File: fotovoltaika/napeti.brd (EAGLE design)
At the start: 46.7 x 49.5 mm, 15 parts, among them X5 JST-XH-04-PIN-LONG-PAD

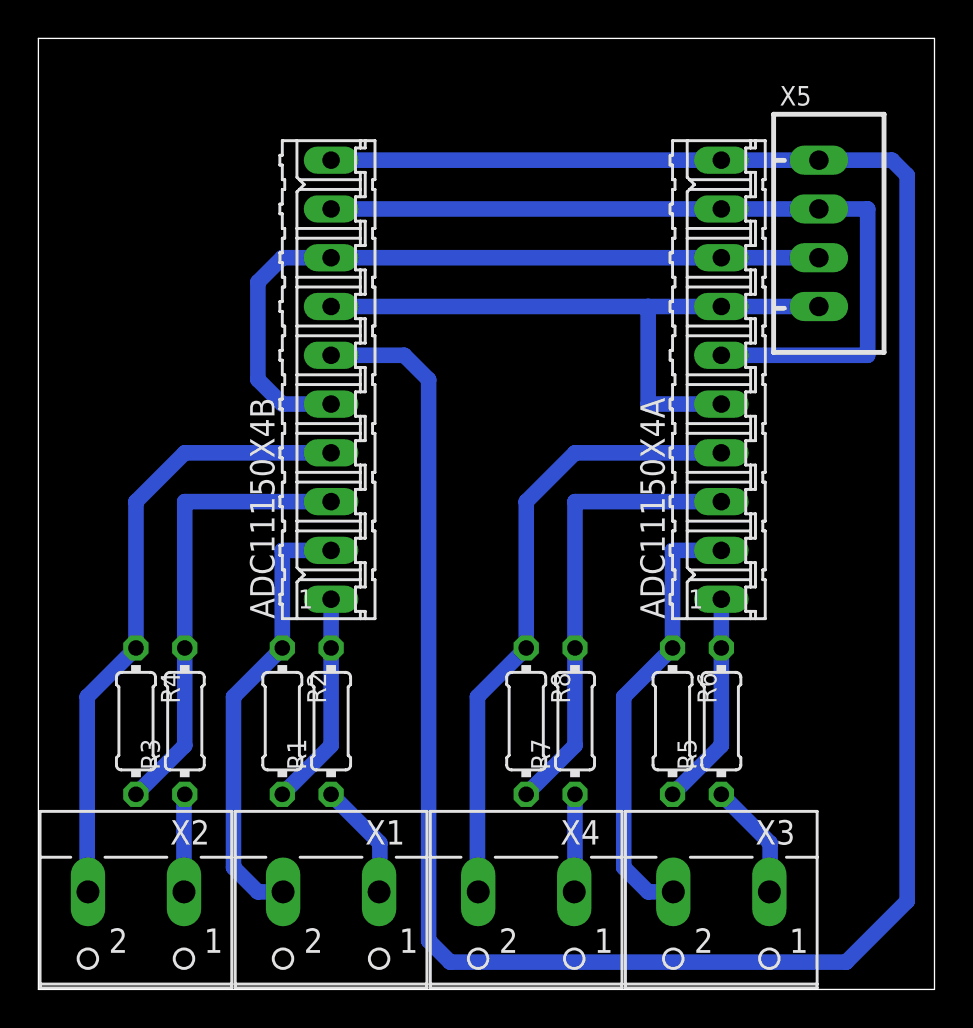
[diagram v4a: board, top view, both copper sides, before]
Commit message: zmena na konektory JST-XH
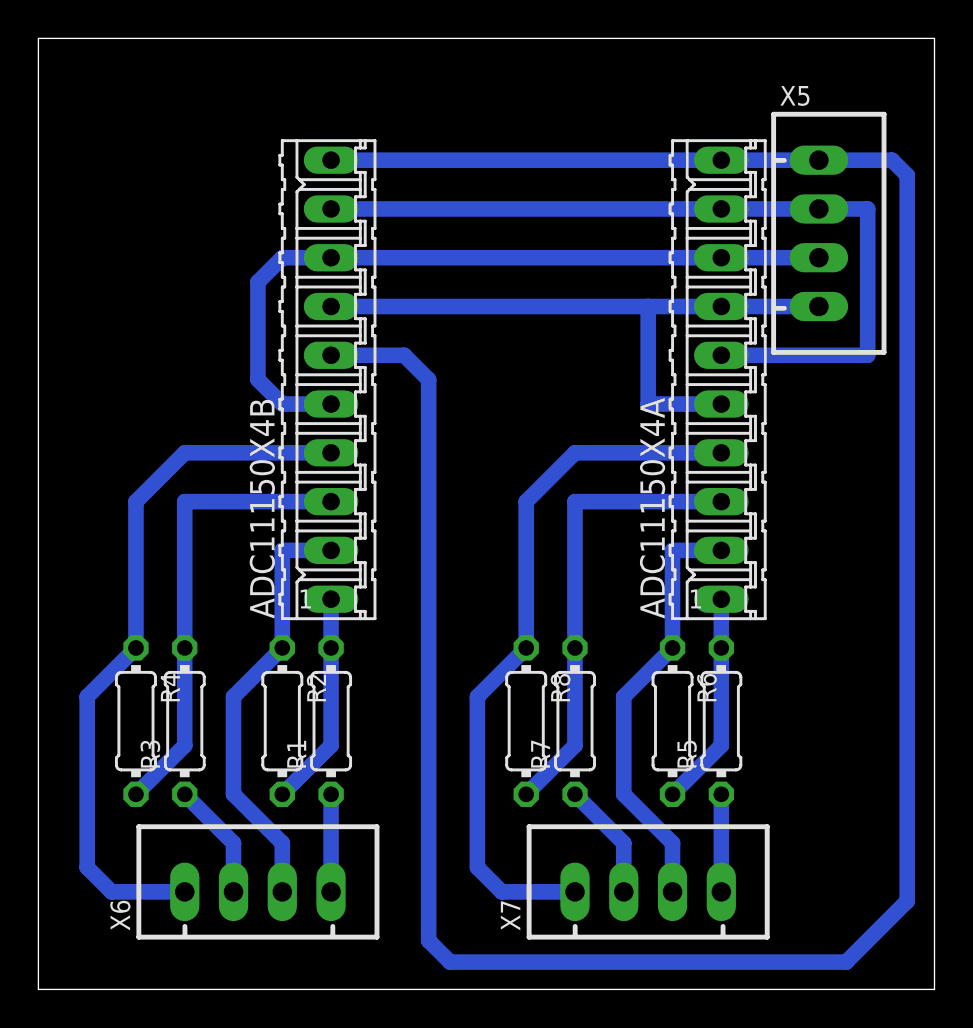
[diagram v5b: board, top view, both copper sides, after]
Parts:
- removed X1, X2, X3, X4: (no value), con-wago-500:W237-102
- added X6, X7: JST-XH-04-PIN-LONG-PAD, Rembrandt:JST-XH-04-PACKAGE-LONG-PAD
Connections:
- net N$10: now also X6.3; no longer X1.2
- net N$14: now also X6.1; no longer X2.2
- net N$2: now also X6.4; no longer X1.1
- net N$3: now also X7.3; no longer X3.2
- net N$5: now also X6.2; no longer X2.1
- net N$6: now also X7.1; no longer X4.2
- net N$7: now also X7.4; no longer X3.1
- net N$8: now also X7.2; no longer X4.1
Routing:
- net N$6: track 32.6 -> 36.9 mm
- net N$14: track 32.6 -> 36.9 mm
- net N$2: track 6.17 -> 5.08 mm
- net N$7: track 6.15 -> 5.08 mm
- net N$5: track 5.10 -> 6.13 mm
- net N$8: track 5.10 -> 6.13 mm
- net N$3: track 23.2 -> 22.4 mm
- net N$10: track 23.2 -> 22.4 mm
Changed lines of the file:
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@@
 <attribute name="VALUE" x="24.9174" y="15.5956" size="0.9906" layer="27" ratio="10" rot="R270"/>
-</element>
-<element name="X1" library="con-wago-500" library_urn="urn:adsk.eagle:library:195" package="W237-102" package3d_urn="urn:adsk.eagle:package:10688/1" value="" x="15.24" y="3.81" smashed="yes" rot="R180">
-<attribute name="MF" value="" x="15.24" y="3.81" size="1.778" layer="27" rot="R180" display="off"/>
-<attribute name="MPN" value="237-102" x="15.24" y="3.81" size="1.778" layer="27" rot="R180" display="off"/>
-<attribute name="NAME" x="19.0862" y="8.8138" size="1.27" layer="25" ratio="10" rot="R180"/>
-<attribute name="OC_FARNELL" value="unknown" x="15.24" y="3.81" size="1.778" layer="27" rot="R180" display="off"/>
-<attribute name="OC_NEWARK" value="70K9898" x="15.24" y="3.81" size="1.778" layer="27" rot="R180" display="off"/>
-<attribute name="VALUE" x="20.28" y="11.43" size="1.27" layer="27" ratio="10" rot="R180"/>
-</element>
-<element name="X2" library="con-wago-500" library_urn="urn:adsk.eagle:library:195" package="W237-102" package3d_urn="urn:adsk.eagle:package:10688/1" value="" x="5.08" y="3.81" smashed="yes" rot="R180">
-<attribute name="MF" value="" x="5.08" y="3.81" size="1.778" layer="27" rot="R180" display="off"/>
-<attribute name="MPN" value="237-102" x="5.08" y="3.81" size="1.778" layer="27" rot="R180" display="off"/>
-<attribute name="NAME" x="8.9262" y="8.8138" size="1.27" layer="25" ratio="10" rot="R180"/>
-<attribute name="OC_FARNELL" value="unknown" x="5.08" y="3.81" size="1.778" layer="27" rot="R180" display="off"/>
-<attribute name="OC_NEWARK" value="70K9898" x="5.08" y="3.81" size="1.778" layer="27" rot="R180" display="off"/>
-<attribute name="VALUE" x="10.12" y="11.43" size="1.27" layer="27" ratio="10" rot="R180"/>
-</element>
-<element name="X3" library="con-wago-500" library_urn="urn:adsk.eagle:library:195" package="W237-102" package3d_urn="urn:adsk.eagle:package:10688/1" value="" x="35.56" y="3.81" smashed="yes" rot="R180">
-<attribute name="MF" value="" x="35.56" y="3.81" size="1.778" layer="27" rot="R180" display="off"/>
-<attribute name="MPN" value="237-102" x="35.56" y="3.81" size="1.778" layer="27" rot="R180" display="off"/>
-<attribute name="NAME" x="39.4062" y="8.8138" size="1.27" layer="25" ratio="10" rot="R180"/>
-<attribute name="OC_FARNELL" value="unknown" x="35.56" y="3.81" size="1.778" layer="27" rot="R180" display="off"/>
-<attribute name="OC_NEWARK" value="70K9898" x="35.56" y="3.81" size="1.778" layer="27" rot="R180" display="off"/>
-<attribute name="VALUE" x="40.6" y="11.43" size="1.27" layer="27" ratio="10" rot="R180"/>
-</element>
-<element name="X4" library="con-wago-500" library_urn="urn:adsk.eagle:library:195" package="W237-102" package3d_urn="urn:adsk.eagle:package:10688/1" value="" x="25.4" y="3.81" smashed="yes" rot="R180">
-<attribute name="MF" value="" x="25.4" y="3.81" size="1.778" layer="27" rot="R180" display="off"/>
-<attribute name="MPN" value="237-102" x="25.4" y="3.81" size="1.778" layer="27" rot="R180" display="off"/>
-<attribute name="NAME" x="29.2462" y="8.8138" size="1.27" layer="25" ratio="10" rot="R180"/>
-<attribute name="OC_FARNELL" value="unknown" x="25.4" y="3.81" size="1.778" layer="27" rot="R180" display="off"/>
-<attribute name="OC_NEWARK" value="70K9898" x="25.4" y="3.81" size="1.778" layer="27" rot="R180" display="off"/>
-<attribute name="VALUE" x="30.44" y="11.43" size="1.27" layer="27" ratio="10" rot="R180"/>
 </element>
 <element name="X5" library="Rembrandt" package="JST-XH-04-PACKAGE-LONG-PAD" value="JST-XH-04-PIN-LONG-PAD" x="40.64" y="39.37" smashed="yes" rot="R270">
 <attribute name="NAME" x="38.6" y="46.025" size="1.016" layer="25" ratio="10"/>
 <attribute name="VALUE" x="44.5325" y="45.3725" size="1.016" layer="27" ratio="10" rot="R270"/>
+</element>
+<element name="X6" library="Rembrandt" package="JST-XH-04-PACKAGE-LONG-PAD" value="JST-XH-04-PIN-LONG-PAD" x="11.43" y="5.08" smashed="yes">
+<attribute name="NAME" x="4.775" y="3.04" size="1.016" layer="25" ratio="10" rot="R90"/>
+<attribute name="VALUE" x="5.4275" y="8.9725" size="1.016" layer="27" ratio="10"/>
+</element>
+<element name="X7" library="Rembrandt" package="JST-XH-04-PACKAGE-LONG-PAD" value="JST-XH-04-PIN-LONG-PAD" x="31.75" y="5.08" smashed="yes">
+<attribute name="NAME" x="25.095" y="3.04" size="1.016" layer="25" ratio="10" rot="R90"/>
+<attribute name="VALUE" x="25.7475" y="8.9725" size="1.016" layer="27" ratio="10"/>
 </element>
 </elements>
@@
 <wire x1="12.7" y1="17.78" x2="12.7" y2="22.86" width="0.8128" layer="16"/>
 <wire x1="12.7" y1="22.86" x2="15.24" y2="22.86" width="0.8128" layer="16"/>
-<wire x1="12.7" y1="17.78" x2="10.16" y2="15.24" width="0.8128" layer="16"/>
-<contactref element="X1" pad="2"/>
-<wire x1="10.16" y1="15.24" x2="10.16" y2="6.35" width="0.8128" layer="16"/>
-<wire x1="10.16" y1="6.35" x2="11.43" y2="5.08" width="0.8128" layer="16"/>
-<wire x1="11.43" y1="5.08" x2="12.74" y2="5.08" width="0.8128" layer="16"/>
+<wire x1="10.16" y1="15.24" x2="12.7" y2="17.78" width="0.8128" layer="16"/>
+<contactref element="X6" pad="3"/>
+<wire x1="12.7" y1="5.08" x2="12.7" y2="7.62" width="0.8128" layer="16"/>
+<wire x1="12.7" y1="7.62" x2="10.16" y2="10.16" width="0.8128" layer="16"/>
+<wire x1="10.16" y1="10.16" x2="10.16" y2="15.24" width="0.8128" layer="16"/>
 </signal>
 <signal name="N$13">
@@
 <wire x1="5.08" y1="25.4" x2="7.62" y2="27.94" width="0.8128" layer="16"/>
 <wire x1="7.62" y1="27.94" x2="15.24" y2="27.94" width="0.8128" layer="16"/>
-<wire x1="5.08" y1="17.78" x2="2.54" y2="15.24" width="0.8128" layer="16"/>
-<contactref element="X2" pad="2"/>
-<wire x1="2.54" y1="15.24" x2="2.54" y2="5.08" width="0.8128" layer="16"/>
-<wire x1="2.54" y1="5.08" x2="2.58" y2="5.08" width="0.8128" layer="16"/>
+<wire x1="2.54" y1="15.24" x2="5.08" y2="17.78" width="0.8128" layer="16"/>
+<contactref element="X6" pad="1"/>
+<wire x1="7.62" y1="5.08" x2="3.81" y2="5.08" width="0.8128" layer="16"/>
+<wire x1="3.81" y1="5.08" x2="2.54" y2="6.35" width="0.8128" layer="16"/>
+<wire x1="2.54" y1="6.35" x2="2.54" y2="15.24" width="0.8128" layer="16"/>
 </signal>
 <signal name="N$2">
 <contactref element="R1" pad="1"/>
-<contactref element="X1" pad="1"/>
-<wire x1="15.24" y1="10.16" x2="17.78" y2="7.62" width="0.8128" layer="16"/>
-<wire x1="17.78" y1="7.62" x2="17.78" y2="5.08" width="0.8128" layer="16"/>
-<wire x1="17.78" y1="5.08" x2="17.74" y2="5.08" width="0.8128" layer="16"/>
+<contactref element="X6" pad="4"/>
+<wire x1="15.24" y1="5.08" x2="15.24" y2="10.16" width="0.8128" layer="16"/>
 </signal>
 <signal name="N$5">
 <contactref element="R3" pad="1"/>
-<contactref element="X2" pad="1"/>
-<wire x1="7.62" y1="10.16" x2="7.58" y2="10.12" width="0.8128" layer="16"/>
-<wire x1="7.58" y1="10.12" x2="7.58" y2="5.08" width="0.8128" layer="16"/>
+<contactref element="X6" pad="2"/>
+<wire x1="10.16" y1="7.62" x2="10.16" y2="5.08" width="0.8128" layer="16"/>
+<wire x1="7.62" y1="10.16" x2="10.16" y2="7.62" width="0.8128" layer="16"/>
 </signal>
 <signal name="N$1">
@@
 <wire x1="33.02" y1="17.78" x2="33.02" y2="22.86" width="0.8128" layer="16"/>
 <wire x1="33.02" y1="22.86" x2="35.56" y2="22.86" width="0.8128" layer="16"/>
-<wire x1="33.02" y1="17.78" x2="30.48" y2="15.24" width="0.8128" layer="16"/>
-<contactref element="X3" pad="2"/>
-<wire x1="30.48" y1="15.24" x2="30.48" y2="6.35" width="0.8128" layer="16"/>
-<wire x1="30.48" y1="6.35" x2="31.75" y2="5.08" width="0.8128" layer="16"/>
-<wire x1="31.75" y1="5.08" x2="33.06" y2="5.08" width="0.8128" layer="16"/>
+<wire x1="30.48" y1="15.24" x2="33.02" y2="17.78" width="0.8128" layer="16"/>
+<contactref element="X7" pad="3"/>
+<wire x1="33.02" y1="5.08" x2="33.02" y2="7.62" width="0.8128" layer="16"/>
+<wire x1="33.02" y1="7.62" x2="30.48" y2="10.16" width="0.8128" layer="16"/>
+<wire x1="30.48" y1="10.16" x2="30.48" y2="15.24" width="0.8128" layer="16"/>
 </signal>
 <signal name="N$4">
@@
 <wire x1="25.4" y1="25.4" x2="27.94" y2="27.94" width="0.8128" layer="16"/>
 <wire x1="27.94" y1="27.94" x2="35.56" y2="27.94" width="0.8128" layer="16"/>
-<wire x1="25.4" y1="17.78" x2="22.86" y2="15.24" width="0.8128" layer="16"/>
-<contactref element="X4" pad="2"/>
-<wire x1="22.86" y1="15.24" x2="22.86" y2="5.12" width="0.8128" layer="16"/>
-<wire x1="22.86" y1="5.12" x2="22.9" y2="5.08" width="0.8128" layer="16"/>
+<wire x1="22.86" y1="15.24" x2="25.4" y2="17.78" width="0.8128" layer="16"/>
+<contactref element="X7" pad="1"/>
+<wire x1="27.94" y1="5.08" x2="24.13" y2="5.08" width="0.8128" layer="16"/>
+<wire x1="24.13" y1="5.08" x2="22.86" y2="6.35" width="0.8128" layer="16"/>
+<wire x1="22.86" y1="6.35" x2="22.86" y2="15.24" width="0.8128" layer="16"/>
 </signal>
 <signal name="N$7">
 <contactref element="R5" pad="1"/>
-<contactref element="X3" pad="1"/>
-<wire x1="35.56" y1="10.16" x2="38.1" y2="7.62" width="0.8128" layer="16"/>
-<wire x1="38.1" y1="7.62" x2="38.1" y2="5.12" width="0.8128" layer="16"/>
-<wire x1="38.1" y1="5.12" x2="38.06" y2="5.08" width="0.8128" layer="16"/>
+<contactref element="X7" pad="4"/>
+<wire x1="35.56" y1="10.16" x2="35.56" y2="5.08" width="0.8128" layer="16"/>
 </signal>
 <signal name="N$8">
 <contactref element="R7" pad="1"/>
-<contactref element="X4" pad="1"/>
-<wire x1="27.94" y1="10.16" x2="27.94" y2="5.12" width="0.8128" layer="16"/>
-<wire x1="27.94" y1="5.12" x2="27.9" y2="5.08" width="0.8128" layer="16"/>
+<contactref element="X7" pad="2"/>
+<wire x1="30.48" y1="5.08" x2="30.48" y2="7.62" width="0.8128" layer="16"/>
+<wire x1="30.48" y1="7.62" x2="27.94" y2="10.16" width="0.8128" layer="16"/>
 </signal>
 </signals>

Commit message: zmena delicu
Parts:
- R1: value 15k -> 10k
- R3: value 10k -> 6k8
- R4: value 4k7 -> 2k2
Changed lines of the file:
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@@
 <attribute name="VALUE" x="19.0754" y="19.304" size="1.27" layer="27" ratio="10" rot="R90"/>
 </element>
-<element name="R1" library="rcl" library_urn="urn:adsk.eagle:library:334" package="0204/7" package3d_urn="urn:adsk.eagle:package:23498/1" value="15k" x="15.24" y="13.97" smashed="yes" rot="R90">
+<element name="R1" library="rcl" library_urn="urn:adsk.eagle:library:334" package="0204/7" package3d_urn="urn:adsk.eagle:package:23498/1" value="10k" x="15.24" y="13.97" smashed="yes" rot="R90">
 <attribute name="NAME" x="13.9446" y="11.43" size="0.9906" layer="25" ratio="10" rot="R90"/>
 <attribute name="SPICEPREFIX" value="R" x="41.91" y="48.26" size="1.778" layer="27" rot="R90" display="off"/>
@@
 <attribute name="VALUE" x="12.2174" y="15.5956" size="0.9906" layer="27" ratio="10" rot="R270"/>
 </element>
-<element name="R3" library="rcl" library_urn="urn:adsk.eagle:library:334" package="0204/7" package3d_urn="urn:adsk.eagle:package:23498/1" value="10k" x="7.62" y="13.97" smashed="yes" rot="R90">
+<element name="R3" library="rcl" library_urn="urn:adsk.eagle:library:334" package="0204/7" package3d_urn="urn:adsk.eagle:package:23498/1" value="6k8" x="7.62" y="13.97" smashed="yes" rot="R90">
 <attribute name="NAME" x="6.3246" y="11.43" size="0.9906" layer="25" ratio="10" rot="R90"/>
 <attribute name="SPICEPREFIX" value="R" x="41.91" y="41.91" size="1.778" layer="27" rot="R90" display="off"/>
 <attribute name="VALUE" x="8.1026" y="12.3444" size="0.9906" layer="27" ratio="10" rot="R90"/>
 </element>
-<element name="R4" library="rcl" library_urn="urn:adsk.eagle:library:334" package="0204/7" package3d_urn="urn:adsk.eagle:package:23498/1" value="4k7" x="5.08" y="13.97" smashed="yes" rot="R270">
+<element name="R4" library="rcl" library_urn="urn:adsk.eagle:library:334" package="0204/7" package3d_urn="urn:adsk.eagle:package:23498/1" value="2k2" x="5.08" y="13.97" smashed="yes" rot="R270">
 <attribute name="NAME" x="6.3754" y="16.51" size="0.9906" layer="25" ratio="10" rot="R270"/>
 <attribute name="SPICEPREFIX" value="R" x="-29.21" y="-24.13" size="1.778" layer="27" rot="R270" display="off"/>

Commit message: +
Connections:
- net SCL: no longer ADC11150X4A.5
- net SDA: no longer ADC11150X4B.5
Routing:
- net SDA: track 39.2 -> 25.4 mm
- net SCL: track 34.3 -> 25.4 mm
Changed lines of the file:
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@@
 <contactref element="ADC11150X4A" pad="8"/>
 <wire x1="35.56" y1="38.1" x2="15.24" y2="38.1" width="0.8128" layer="16"/>
-<contactref element="ADC11150X4B" pad="5"/>
-<wire x1="15.24" y1="30.48" x2="12.7" y2="30.48" width="0.8128" layer="16"/>
-<wire x1="12.7" y1="30.48" x2="11.43" y2="31.75" width="0.8128" layer="16"/>
-<wire x1="11.43" y1="31.75" x2="11.43" y2="36.83" width="0.8128" layer="16"/>
-<wire x1="11.43" y1="36.83" x2="12.7" y2="38.1" width="0.8128" layer="16"/>
-<wire x1="12.7" y1="38.1" x2="15.24" y2="38.1" width="0.8128" layer="16"/>
 <contactref element="X5" pad="3"/>
 <wire x1="35.56" y1="38.1" x2="40.64" y2="38.1" width="0.8128" layer="16"/>
@@
 <contactref element="ADC11150X4B" pad="7"/>
 <contactref element="ADC11150X4A" pad="7"/>
-<wire x1="35.56" y1="35.56" x2="31.75" y2="35.56" width="0.8128" layer="16"/>
-<wire x1="31.75" y1="35.56" x2="15.24" y2="35.56" width="0.8128" layer="16"/>
-<contactref element="ADC11150X4A" pad="5"/>
-<wire x1="35.56" y1="30.48" x2="31.75" y2="30.48" width="0.8128" layer="16"/>
-<wire x1="31.75" y1="30.48" x2="31.75" y2="35.56" width="0.8128" layer="16"/>
+<wire x1="35.56" y1="35.56" x2="15.24" y2="35.56" width="0.8128" layer="16"/>
 <contactref element="X5" pad="4"/>
 <wire x1="35.56" y1="35.56" x2="40.64" y2="35.56" width="0.8128" layer="16"/>
